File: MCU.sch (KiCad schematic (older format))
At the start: 11 parts, among them U2 FM24CL16B, U3 STM32F401RCTx, Y1 20Mhz

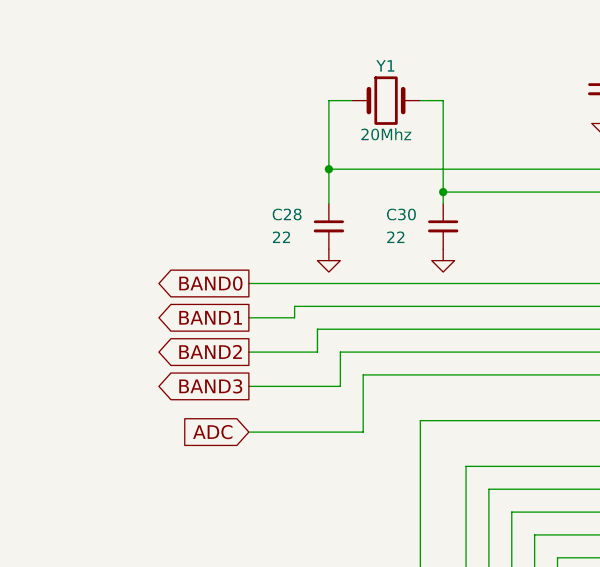
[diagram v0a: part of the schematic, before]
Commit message: TODO: power supplay connector
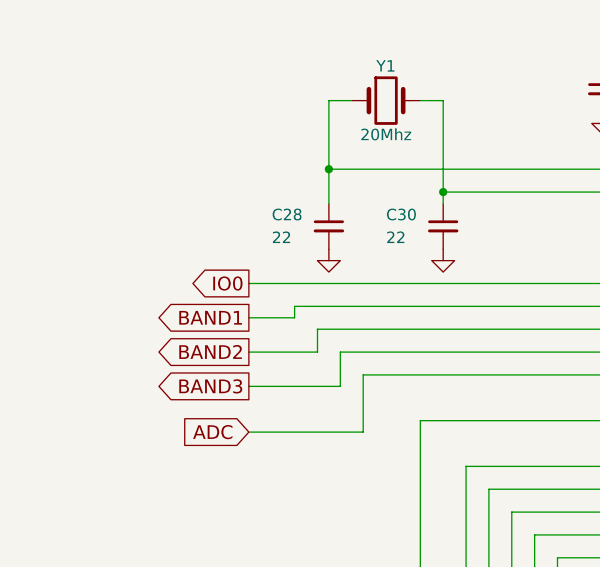
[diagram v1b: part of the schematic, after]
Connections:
- net labels added: IO0
- net labels removed: BAND0

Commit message: first module
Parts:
- added J?: IDC10 Serial Wire, UI:USBBLASTER, symbol Conn_02x05_Odd_Even
- added RN?: 47, Resistors_SMD:R_Array_Convex_4x0603, symbol R_Pack04
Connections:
- net labels added: MCU_VOLTAGE_33V
- net labels removed: PTT_IN
- wire segments 155 -> 180
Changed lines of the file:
@@
 Text GLabel 10000 1600 2    60   Input ~ 0
 ENCODER_A
-Text GLabel 4350 7150 0    60   Input ~ 0
+Text GLabel 1100 4850 0    60   Input ~ 0
 KEY_A
 Text GLabel 2050 7150 0    60   Input ~ 0
@@
 Text GLabel 2050 7450 0    60   Input ~ 0
 KEY_D
-Text GLabel 4350 7350 0    60   Input ~ 0
-PTT_IN
+Text GLabel 3950 6300 2    60   Input ~ 0
+MCU_VOLTAGE_33V
 Text GLabel 1700 4100 0    60   Input ~ 0
 ADC
@@
 Text GLabel 10000 1100 2    60   Output ~ 0
 LINE_OUT_RIGHT_MCU
-Text GLabel 4700 6700 0    60   Input ~ 0
+Text GLabel 1150 5200 0    60   Input ~ 0
 KEY_CW
 Wire Wire Line
@@
 	1    0    0    -1
 $EndComp
+$Comp
+L Conn_02x05_Odd_Even J?
+U 1 1 5EAA5CD3
+P 4300 6800
+F 0 "J?" H 4350 7100 50  0000 C CNN
+F 1 "IDC10 Serial Wire" H 4350 6500 50  0000 C CNN
+F 2 "UI:USBBLASTER" H 4300 6800 50  0001 C CNN
+F 3 "" H 4300 6800 50  0001 C CNN
+	1    4300 6800
+	1    0    0    -1
+$EndComp
+$Comp
+L R_Pack04 RN?
+U 1 1 5EAA5CDA
+P 5500 6800
+F 0 "RN?" V 5200 6800 50  0000 C CNN
+F 1 "47" V 5700 6800 50  0000 C CNN
+F 2 "Resistors_SMD:R_Array_Convex_4x0603" V 5775 6800 50  0001 C CNN
+F 3 "" H 5500 6800 50  0001 C CNN
+	1    5500 6800
+	0    1    1    0
+$EndComp
+Wire Wire Line
+	4600 6600 5300 6600
+Wire Wire Line
+	4600 6700 5300 6700
+Wire Wire Line
+	4600 6800 5300 6800
+Wire Wire Line
+	4600 7000 4900 7000
+Wire Wire Line
+	4900 7000 4900 6900
+Wire Wire Line
+	4900 6900 5300 6900
+Text GLabel 6150 6450 2    60   BiDi ~ 0
+SWDIO
+Text GLabel 6150 6650 2    60   BiDi ~ 0
+SWCLK
+Text GLabel 6150 6850 2    60   BiDi ~ 0
+SWO
+Text GLabel 6150 7050 2    60   Output ~ 0
+MCU_RESET
+Wire Wire Line
+	5700 6600 5800 6600
+Wire Wire Line
+	5800 6600 5800 6450
+Wire Wire Line
+	5800 6450 6150 6450
+Wire Wire Line
+	5700 6700 5900 6700
+Wire Wire Line
+	5900 6700 5900 6650
+Wire Wire Line
+	5900 6650 6150 6650
+Wire Wire Line
+	5700 6800 5900 6800
+Wire Wire Line
+	5900 6800 5900 6850
+Wire Wire Line
+	5900 6850 6150 6850
+Wire Wire Line
+	5700 6900 5800 6900
+Wire Wire Line
+	5800 6900 5800 7050
+Wire Wire Line
+	5800 7050 6150 7050
+$Comp
+L GND #PWR?
+U 1 1 5EAA5CF7
+P 3850 7050
+F 0 "#PWR?" H 3850 6800 50  0001 C CNN
+F 1 "GND" H 3850 6900 50  0001 C CNN
+F 2 "" H 3850 7050 50  0001 C CNN
+F 3 "" H 3850 7050 50  0001 C CNN
+	1    3850 7050
+	1    0    0    -1
+$EndComp
+Wire Wire Line
+	3850 6700 3850 7050
+Wire Wire Line
+	3850 7000 4100 7000
+Wire Wire Line
+	3850 6700 4100 6700
+Connection ~ 3850 7000
+Wire Wire Line
+	4100 6800 3850 6800
+Connection ~ 3850 6800
+Wire Wire Line
+	3850 6300 3850 6600
+Wire Wire Line
+	3850 6600 4100 6600
+Wire Wire Line
+	3950 6300 3850 6300
 $EndSCHEMATC

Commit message: add I2S_CLKIN_MCU
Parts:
- gave numbers to parts that had none: 2
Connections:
- net labels added: I2S_CLKIN_MCU
- net labels removed: I2C_SDA_MCU
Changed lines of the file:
@@
 $Descr A4 11693 8268
 encoding utf-8
-Sheet 4 6
+Sheet 4 5
 Title ""
 Date ""
@@
 Text GLabel 10000 1950 2    60   Output ~ 0
 I2C_SCL_MCU
-Text GLabel 2050 6550 0    60   BiDi ~ 0
-I2C_SDA_MCU
+Text GLabel 2050 6550 0    60   Input ~ 0
+I2S_CLKIN_MCU
 Text GLabel 10000 3000 2    60   BiDi ~ 0
 SWDIO
@@
 SWO
 $Comp
-L GND #PWR47
+L GND #PWR039
 U 1 1 5DD650F1
 P 6150 5450
-F 0 "#PWR47" H 6150 5200 50  0001 C CNN
+F 0 "#PWR039" H 6150 5200 50  0001 C CNN
 F 1 "GND" H 6150 5300 50  0001 C CNN
 F 2 "" H 6150 5450 50  0001 C CNN
@@
 $EndComp
 $Comp
-L GND #PWR44
+L GND #PWR040
 U 1 1 5DD65332
 P 3250 2700
-F 0 "#PWR44" H 3250 2450 50  0001 C CNN
+F 0 "#PWR040" H 3250 2450 50  0001 C CNN
 F 1 "GND" H 3250 2550 50  0001 C CNN
 F 2 "" H 3250 2700 50  0001 C CNN
@@
 $EndComp
 $Comp
-L GND #PWR41
+L GND #PWR041
 U 1 1 5DD655DB
 P 2050 3300
-F 0 "#PWR41" H 2050 3050 50  0001 C CNN
+F 0 "#PWR041" H 2050 3050 50  0001 C CNN
 F 1 "GND" H 2050 3150 50  0001 C CNN
 F 2 "" H 2050 3300 50  0001 C CNN
@@
 $EndComp
 $Comp
-L GND #PWR43
+L GND #PWR042
 U 1 1 5DD65924
 P 2750 2100
-F 0 "#PWR43" H 2750 1850 50  0001 C CNN
+F 0 "#PWR042" H 2750 1850 50  0001 C CNN
 F 1 "GND" H 2750 1950 50  0001 C CNN
 F 2 "" H 2750 2100 50  0001 C CNN
@@
 $EndComp
 $Comp
-L GND #PWR39
+L GND #PWR043
 U 1 1 5DD66640
 P 1450 1700
-F 0 "#PWR39" H 1450 1450 50  0001 C CNN
+F 0 "#PWR043" H 1450 1450 50  0001 C CNN
 F 1 "GND" H 1450 1550 50  0001 C CNN
 F 2 "" H 1450 1700 50  0001 C CNN
@@
 $EndComp
 $Comp
-L GND #PWR40
+L GND #PWR044
 U 1 1 5DD667F8
 P 1900 1550
-F 0 "#PWR40" H 1900 1300 50  0001 C CNN
+F 0 "#PWR044" H 1900 1300 50  0001 C CNN
 F 1 "GND" H 1900 1400 50  0001 C CNN
 F 2 "" H 1900 1550 50  0001 C CNN
@@
 I2C_SDA
 $Comp
-L +3V3 #PWR38
+L +3V3 #PWR045
 U 1 1 5DD9FC90
 P 1450 900
-F 0 "#PWR38" H 1450 750 50  0001 C CNN
+F 0 "#PWR045" H 1450 750 50  0001 C CNN
 F 1 "+3V3" H 1450 1050 50  0000 C CNN
 F 2 "" H 1450 900 50  0001 C CNN
@@
 $EndComp
 $Comp
-L GND #PWR37
+L GND #PWR046
 U 1 1 5DDA00B4
 P 900 950
-F 0 "#PWR37" H 900 700 50  0001 C CNN
+F 0 "#PWR046" H 900 700 50  0001 C CNN
 F 1 "GND" H 900 800 50  0001 C CNN
 F 2 "" H 900 950 50  0001 C CNN
@@
 $EndComp
 $Comp
-L +3V3 #PWR46
+L +3V3 #PWR047
 U 1 1 5DDA012B
 P 5550 1300
-F 0 "#PWR46" H 5550 1150 50  0001 C CNN
+F 0 "#PWR047" H 5550 1150 50  0001 C CNN
 F 1 "+3V3" V 5550 1550 50  0000 C CNN
 F 2 "" H 5550 1300 50  0001 C CNN
@@
 $EndComp
 $Comp
-L +3V3 #PWR48
+L +3V3 #PWR048
 U 1 1 5DDA0C93
 P 6600 650
-F 0 "#PWR48" H 6600 500 50  0001 C CNN
+F 0 "#PWR048" H 6600 500 50  0001 C CNN
 F 1 "+3V3" V 6600 900 50  0000 C CNN
 F 2 "" H 6600 650 50  0001 C CNN
@@
 $EndComp
 $Comp
-L GND #PWR49
+L GND #PWR049
 U 1 1 5DDA0E68
 P 6800 900
-F 0 "#PWR49" H 6800 650 50  0001 C CNN
+F 0 "#PWR049" H 6800 650 50  0001 C CNN
 F 1 "GND" H 6800 750 50  0001 C CNN
 F 2 "" H 6800 900 50  0001 C CNN
@@
 $EndComp
 $Comp
-L GND #PWR50
+L GND #PWR050
 U 1 1 5DDA0EDC
 P 7300 900
-F 0 "#PWR50" H 7300 650 50  0001 C CNN
+F 0 "#PWR050" H 7300 650 50  0001 C CNN
 F 1 "GND" H 7300 750 50  0001 C CNN
 F 2 "" H 7300 900 50  0001 C CNN
@@
 $EndComp
 $Comp
-L GND #PWR51
+L GND #PWR051
 U 1 1 5DDA0F4B
 P 7800 900
-F 0 "#PWR51" H 7800 650 50  0001 C CNN
+F 0 "#PWR051" H 7800 650 50  0001 C CNN
 F 1 "GND" H 7800 750 50  0001 C CNN
 F 2 "" H 7800 900 50  0001 C CNN
@@
 TX2
 $Comp
-L GND #PWR45
+L GND #PWR052
 U 1 1 5DDFAF2B
 P 3650 2050
-F 0 "#PWR45" H 3650 1800 50  0001 C CNN
+F 0 "#PWR052" H 3650 1800 50  0001 C CNN
 F 1 "GND" H 3650 1900 50  0001 C CNN
 F 2 "" H 3650 2050 50  0001 C CNN
@@
 	2650 4250 3650 4250
 $Comp
-L GND #PWR42
+L GND #PWR053
 U 1 1 5DD65598
 P 2550 3300
-F 0 "#PWR42" H 2550 3050 50  0001 C CNN
+F 0 "#PWR053" H 2550 3050 50  0001 C CNN
 F 1 "GND" H 2550 3150 50  0001 C CNN
 F 2 "" H 2550 3300 50  0001 C CNN
@@
 $EndComp
 $Comp
-L Conn_02x05_Odd_Even J?
+L Conn_02x05_Odd_Even J6
 U 1 1 5EAA5CD3
 P 4300 6800
-F 0 "J?" H 4350 7100 50  0000 C CNN
+F 0 "J6" H 4350 7100 50  0000 C CNN
 F 1 "IDC10 Serial Wire" H 4350 6500 50  0000 C CNN
 F 2 "UI:USBBLASTER" H 4300 6800 50  0001 C CNN
@@
 $EndComp
 $Comp
-L R_Pack04 RN?
+L R_Pack04 RN8
 U 1 1 5EAA5CDA
 P 5500 6800
-F 0 "RN?" V 5200 6800 50  0000 C CNN
+F 0 "RN8" V 5200 6800 50  0000 C CNN
 F 1 "47" V 5700 6800 50  0000 C CNN
 F 2 "Resistors_SMD:R_Array_Convex_4x0603" V 5775 6800 50  0001 C CNN
@@
 	5800 7050 6150 7050
 $Comp
-L GND #PWR?
+L GND #PWR054
 U 1 1 5EAA5CF7
 P 3850 7050
-F 0 "#PWR?" H 3850 6800 50  0001 C CNN
+F 0 "#PWR054" H 3850 6800 50  0001 C CNN
 F 1 "GND" H 3850 6900 50  0001 C CNN
 F 2 "" H 3850 7050 50  0001 C CNN
@@
 Wire Wire Line
 	3950 6300 3850 6300
+Text GLabel 10650 3700 2    60   Input ~ 0
+I2S_CLKIN_MCU
 $EndSCHEMATC

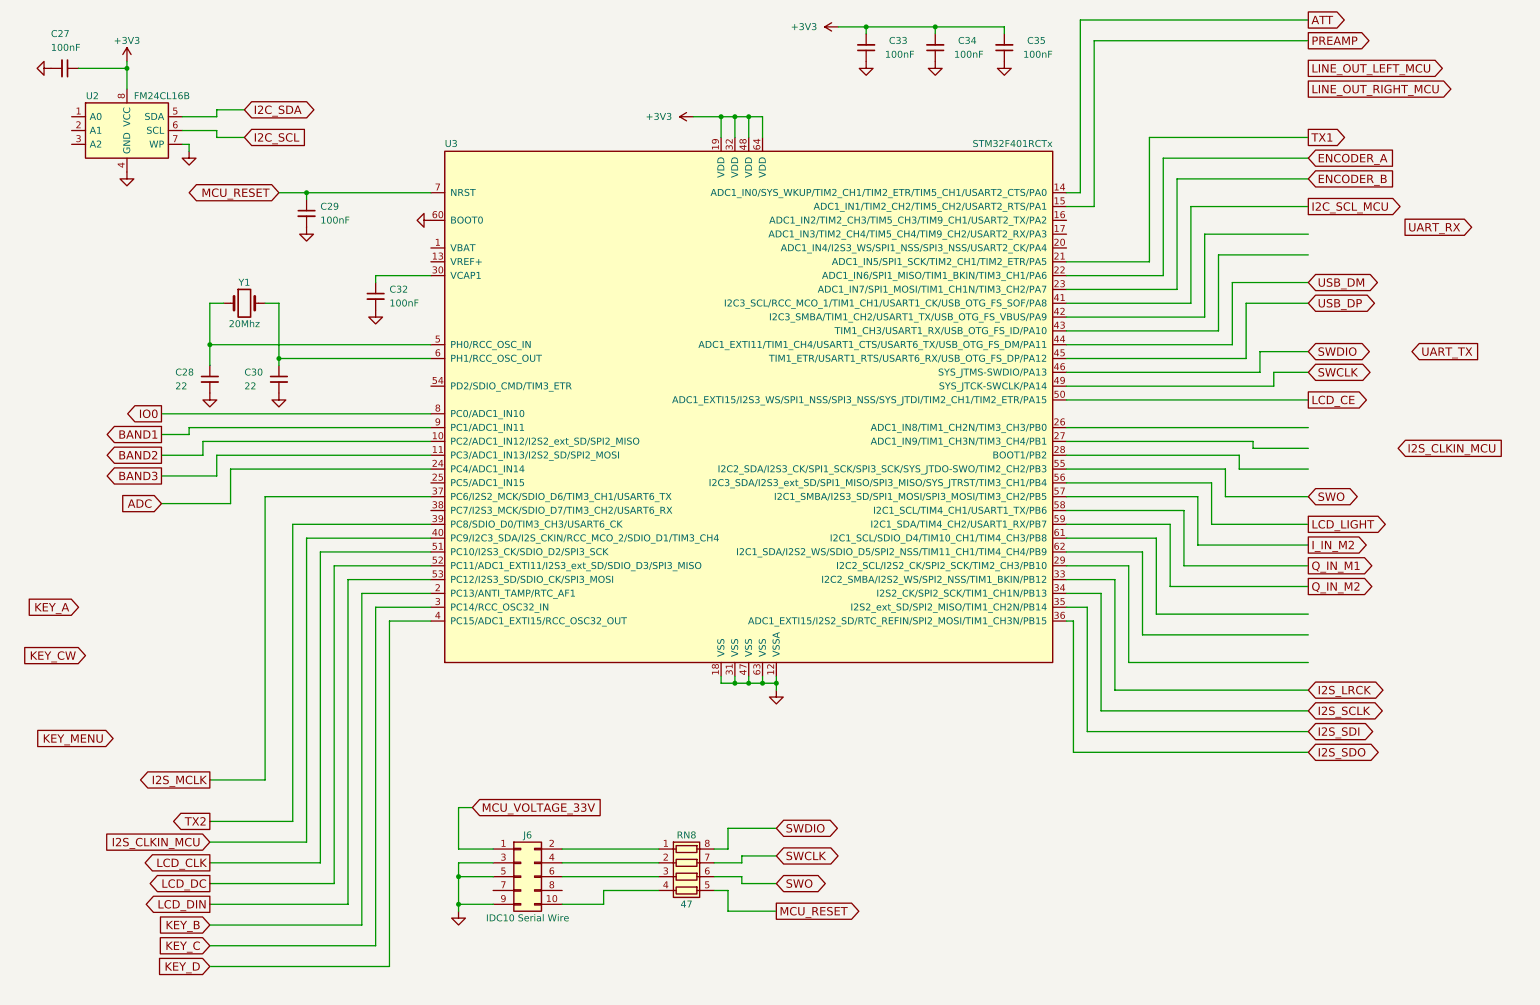
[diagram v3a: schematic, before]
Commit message: PCB almost ready, needs some GND vias
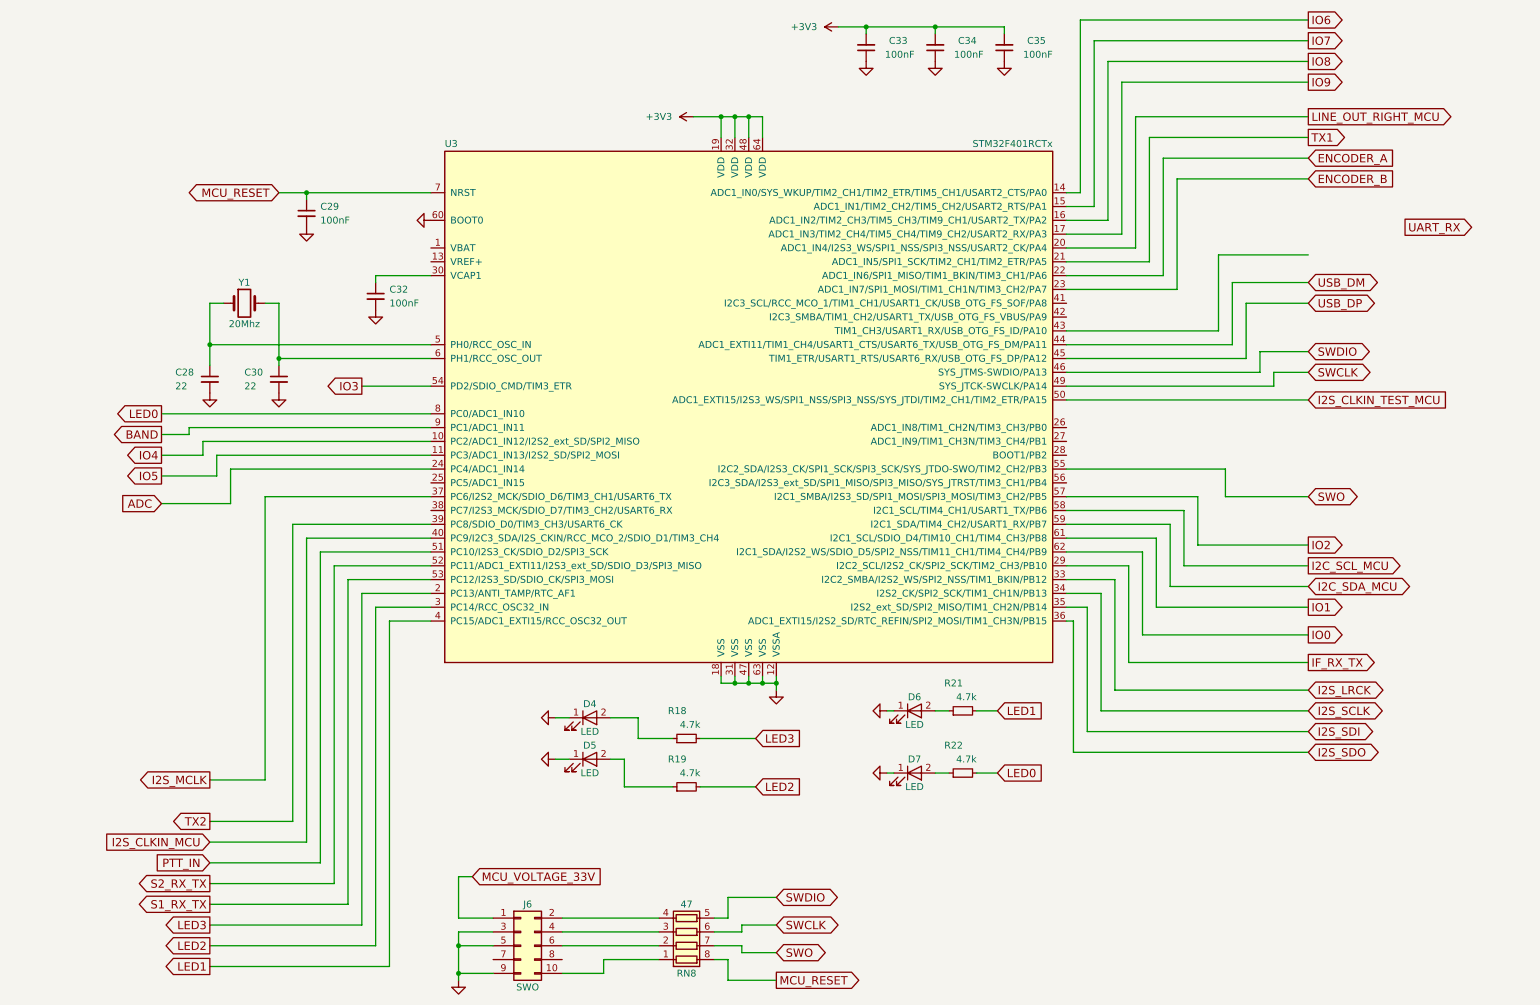
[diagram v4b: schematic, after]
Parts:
- removed C27: 100nF, UI:C_1206_0603, symbol C_Small
- removed U2: FM24CL16B, Housings_SOIC:SOIC-8_3.9x4.9mm_Pitch1.27mm, symbol 24LC16
- added D4, D5, D6, D7: LED, LEDs:LED_D5.0mm_FlatTop, symbol LED
- added R18, R19, R21, R22: 4.7k, Resistors_THT:R_Axial_DIN0204_L3.6mm_D1.6mm_P7.62mm_Horizontal, symbol R_Small
- J6: value IDC10 Serial Wire -> SWO; footprint UI:USBBLASTER -> Pin_Headers:Pin_Header_Straight_2x05_Pitch2.54mm
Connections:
- net labels added: BAND, I2C_SDA_MCU, I2S_CLKIN_TEST_MCU, IF_RX_TX, IO1, IO2, IO3, IO4, IO5, IO6, IO7, IO8, IO9, LED0, LED1, LED2, LED3, PTT_IN, S1_RX_TX, S2_RX_TX
- net labels removed: ATT, BAND1, BAND2, BAND3, I2C_SCL, I2C_SDA, I_IN_M2, KEY_A, KEY_B, KEY_C, KEY_CW, KEY_D, KEY_MENU, LCD_CE, LCD_CLK, LCD_DC, LCD_DIN, LCD_LIGHT, LINE_OUT_LEFT_MCU, PREAMP, Q_IN_M1, Q_IN_M2, UART_TX
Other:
- moved on the sheet: RN8

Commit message: edit
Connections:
- net IO6 is gone; now on net BAND: U3.14 (ADC1_IN0/SYS_WKUP/TIM2_CH1/TIM2_ETR/TIM5_CH1/USART2_CTS/PA0)
- net BAND: no longer U3.9 (PC1/ADC1_IN11)
- net ENCODER_A: no longer names the net of U3.22 (ADC1_IN6/SPI1_MISO/TIM1_BKIN/TIM3_CH1/PA6)
- net ENCODER_B: no longer names the net of U3.23 (ADC1_IN7/SPI1_MOSI/TIM1_CH1N/TIM3_CH2/PA7)
- net LINE_OUT_RIGHT_MCU: no longer names the net of U3.20 (ADC1_IN4/I2S3_WS/SPI1_NSS/SPI3_NSS/USART2_CK/PA4)
- net TX1: no longer names the net of U3.21 (ADC1_IN5/SPI1_SCK/TIM2_CH1/TIM2_ETR/PA5)
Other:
- moved on the sheet: D4, D5
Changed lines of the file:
@@
 	1    0    0    -1
 $EndComp
-Text GLabel 10700 2100 2    60   Output ~ 0
-UART_RX
 Text GLabel 10000 3350 2    60   Input ~ 0
 I2S_CLKIN_TEST_MCU
-Text GLabel 10000 1750 2    60   Input ~ 0
-ENCODER_B
-Text GLabel 10000 1600 2    60   Input ~ 0
-ENCODER_A
 Text GLabel 3950 6800 2    60   Input ~ 0
 MCU_VOLTAGE_33V
@@
 Text GLabel 1700 3750 0    60   Output ~ 0
 IO4
-Text GLabel 10000 600  2    60   Output ~ 0
-IO6
 Text GLabel 10000 750  2    60   Output ~ 0
 IO7
@@
 Text GLabel 1700 3900 0    60   Output ~ 0
 IO5
-Text GLabel 10000 1450 2    60   Output ~ 0
-TX1
 Text GLabel 2050 6400 0    60   Output ~ 0
 TX2
@@
 	1    0    0    -1
 $EndComp
-Text GLabel 1700 3600 0    60   Output ~ 0
+Text GLabel 10000 600  2    60   Output ~ 0
 BAND
-Text GLabel 10000 1300 2    60   Output ~ 0
-LINE_OUT_RIGHT_MCU
 Wire Wire Line
 	2450 4050 3650 4050
@@
 	8250 3350 10000 3350
 Wire Wire Line
-	8850 2350 8250 2350
-Wire Wire Line
-	8250 2450 8950 2450
-Wire Wire Line
-	9050 2550 8250 2550
-Wire Wire Line
-	9350 2850 8250 2850
-Wire Wire Line
 	9450 2950 8250 2950
 Wire Wire Line
@@
 Wire Wire Line
 	9450 2500 9450 2950
-Wire Wire Line
-	10000 2300 9350 2300
-Wire Wire Line
-	9350 2300 9350 2850
-Wire Wire Line
-	10000 1750 9050 1750
-Wire Wire Line
-	9050 1750 9050 2550
-Wire Wire Line
-	10000 1600 8950 1600
-Wire Wire Line
-	8950 1600 8950 2450
-Wire Wire Line
-	10000 1450 8850 1450
-Wire Wire Line
-	8850 1450 8850 2350
 Wire Wire Line
 	8450 1950 8450 750
@@
 Wire Wire Line
 	1700 3450 3650 3450
-Wire Wire Line
-	1700 3600 1900 3600
-Wire Wire Line
-	1900 3600 1900 3550
-Wire Wire Line
-	1900 3550 3650 3550
 Wire Wire Line
 	1700 3750 2000 3750
@@
 L LED D4
 U 1 1 5EAAAB57
-P 4800 5650
-F 0 "D4" H 4800 5750 50  0000 C CNN
-F 1 "LED" H 4800 5550 50  0000 C CNN
-F 2 "LEDs:LED_D5.0mm_FlatTop" H 4800 5650 50  0001 C CNN
-F 3 "" H 4800 5650 50  0001 C CNN
-	1    4800 5650
+P 4900 5800
+F 0 "D4" H 4900 5900 50  0000 C CNN
+F 1 "LED" H 4900 5700 50  0000 C CNN
+F 2 "LEDs:LED_D5.0mm_FlatTop" H 4900 5800 50  0001 C CNN
+F 3 "" H 4900 5800 50  0001 C CNN
+	1    4900 5800
 	1    0    0    -1
 $EndComp
@@
 L LED D5
 U 1 1 5EAAABEF
-P 4800 5950
-F 0 "D5" H 4800 6050 50  0000 C CNN
-F 1 "LED" H 4800 5850 50  0000 C CNN
-F 2 "LEDs:LED_D5.0mm_FlatTop" H 4800 5950 50  0001 C CNN
-F 3 "" H 4800 5950 50  0001 C CNN
-	1    4800 5950
+P 4900 6150
+F 0 "D5" H 4900 6250 50  0000 C CNN
+F 1 "LED" H 4900 6050 50  0000 C CNN
+F 2 "LEDs:LED_D5.0mm_FlatTop" H 4900 6150 50  0001 C CNN
+F 3 "" H 4900 6150 50  0001 C CNN
+	1    4900 6150
 	1    0    0    -1
 $EndComp
@@
 L GND #PWR054
 U 1 1 5EAAAE5C
-P 4550 5950
-F 0 "#PWR054" H 4550 5700 50  0001 C CNN
-F 1 "GND" H 4550 5800 50  0001 C CNN
-F 2 "" H 4550 5950 50  0001 C CNN
-F 3 "" H 4550 5950 50  0001 C CNN
-	1    4550 5950
+P 4600 6150
+F 0 "#PWR054" H 4600 5900 50  0001 C CNN
+F 1 "GND" H 4600 6000 50  0001 C CNN
+F 2 "" H 4600 6150 50  0001 C CNN
+F 3 "" H 4600 6150 50  0001 C CNN
+	1    4600 6150
 	0    1    1    0
 $EndComp
 Wire Wire Line
-	4650 5650 4550 5650
-Wire Wire Line
-	4650 5950 4550 5950
-Wire Wire Line
-	4950 5950 5050 5950
-Wire Wire Line
-	5050 5950 5050 6150
+	4750 5800 4600 5800
+Wire Wire Line
+	4750 6150 4600 6150
 Wire Wire Line
 	5050 6150 5400 6150
-Wire Wire Line
-	5150 5650 4950 5650
 Wire Wire Line
 	5600 6150 6000 6150
@@
 Text GLabel 2050 7000 0    60   Output ~ 0
 S1_RX_TX
-Wire Wire Line
-	8250 2250 8750 2250
-Wire Wire Line
-	8750 2250 8750 1300
-Wire Wire Line
-	8750 1300 10000 1300
 Text GLabel 2050 7150 0    60   Output ~ 0
 LED3
@@
 	5600 5800 6000 5800
 Wire Wire Line
-	5400 5800 5150 5800
-Wire Wire Line
-	5150 5800 5150 5650
+	5050 5800 5400 5800
 $Comp
 L R_Small R19
@@
 L GND #PWR057
 U 1 1 5EBBA1A1
-P 4550 5650
-F 0 "#PWR057" H 4550 5400 50  0001 C CNN
-F 1 "GND" H 4550 5500 50  0001 C CNN
-F 2 "" H 4550 5650 50  0001 C CNN
-F 3 "" H 4550 5650 50  0001 C CNN
-	1    4550 5650
+P 4600 5800
+F 0 "#PWR057" H 4600 5550 50  0001 C CNN
+F 1 "GND" H 4600 5650 50  0001 C CNN
+F 2 "" H 4600 5800 50  0001 C CNN
+F 3 "" H 4600 5800 50  0001 C CNN
+	1    4600 5800
 	0    1    1    0
 $EndComp
